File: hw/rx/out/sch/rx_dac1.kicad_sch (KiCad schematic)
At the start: 13 parts, among them U3 PCM5102A

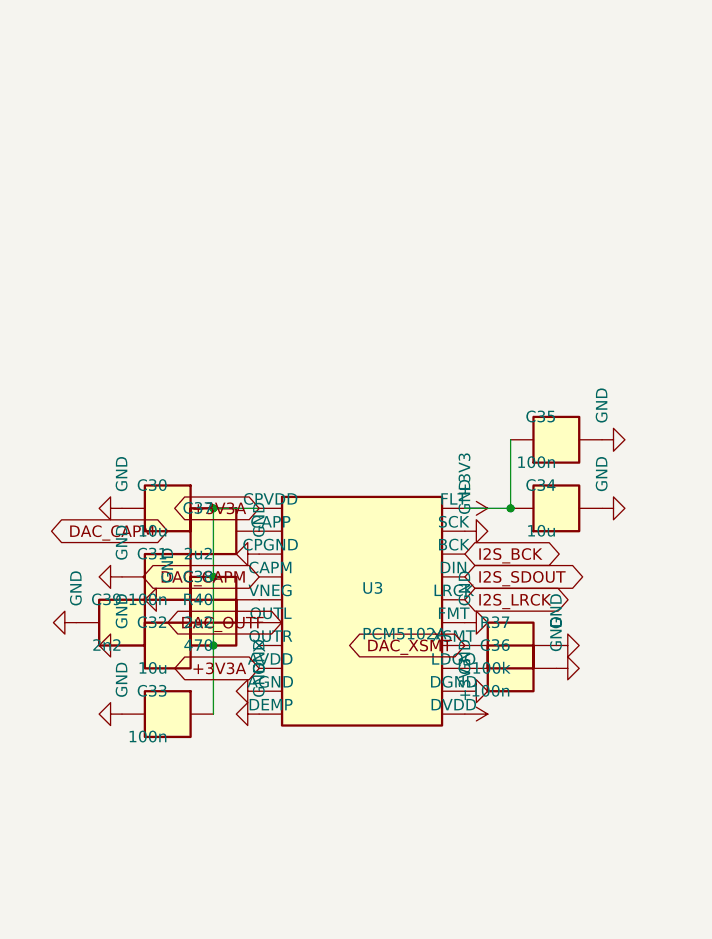
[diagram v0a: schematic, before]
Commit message: hw/rx: review fixes for #81 (mute relay + supervisor, S1J clamps, VCM discharge + 2-pole filter, 16 V LDOs, keyed header, I2S DNP, cable stability + power-cycle SPICE, FLT low latency) (#32)
Co-Authored-By: Claude Opus 5.5 <noreply@anthropic.com>
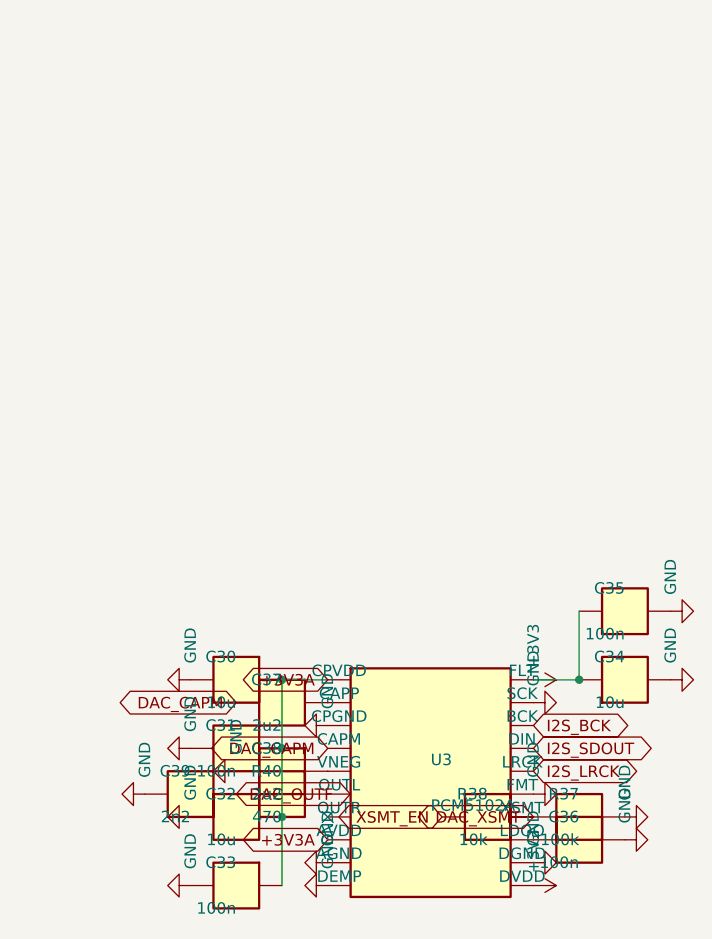
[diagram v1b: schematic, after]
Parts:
- added R38: 10k, Resistor_SMD:R_0402_1005Metric, symbol openpack_rx:R
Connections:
- net DAC_XSMT: now also R38.2
- new net XSMT_EN: R38.1
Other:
- moved on the sheet: C30, C31, C32, C33, C34, C35, C36, C37, C38, C39, R37, R40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

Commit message: hw/rx: receiver module BT40NE -> BT40E, FEM node pack-only (ADR-0021, #112)
- hw/rx: BT40E symbol (Fanstel v1.09 p.14 pad map = BT40F/NE names), footprint
  openpack:Fanstel_BT40E (14x16 mm), no FEM nets, P1.05 open; GPIO map unchanged.
  ERC 0/0. BOM: Digi-Key UK GBP 9.7765 q100 -> $30.68 / GBP 23.38 per sub-board.
- fw: receiver builds add boards/role_rx_cpunet.overlay (FEM node disabled, no
  &radio fem); rx.c refuses to build with the FEM enabled.
- ADR-0014 amended (datasheet checks, FCC X8WBT40F, no UKCA DoC, BOM).

Co-Authored-By: Claude Opus 5.5 <noreply@anthropic.com>
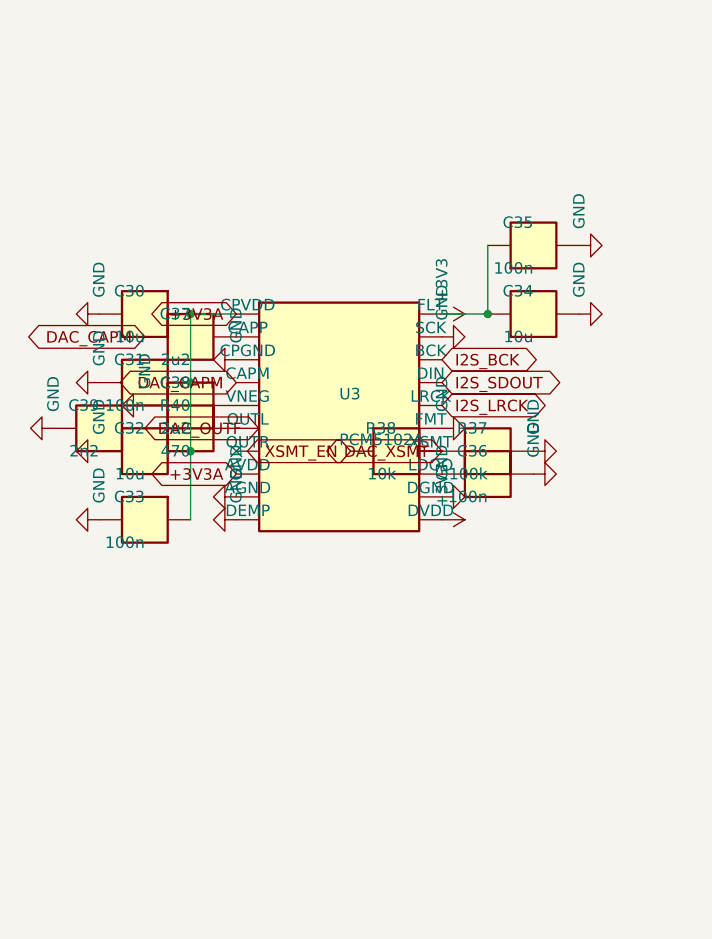
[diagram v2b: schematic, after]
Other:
- moved on the sheet: C30, C31, C32, C33, C34, C35, C36, C37, C38, C39, R37, R38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

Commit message: hw/rx: receiver sub-board layout, 50 ohm GCPW, keyed J1, JLC rules that load, fab outputs (#34) (#116)
Part of #34. Receiver layout (48x90 mm, DRC 0/0), #116 independent-review fixes (netclass pour clearances in rx + pack, no hole at J1 pin 14, solid RF grounds, K1 pin-1/CPL), every placed part with a checked LCSC code.

Co-Authored-By: Claude Opus 5.5 <noreply@anthropic.com>
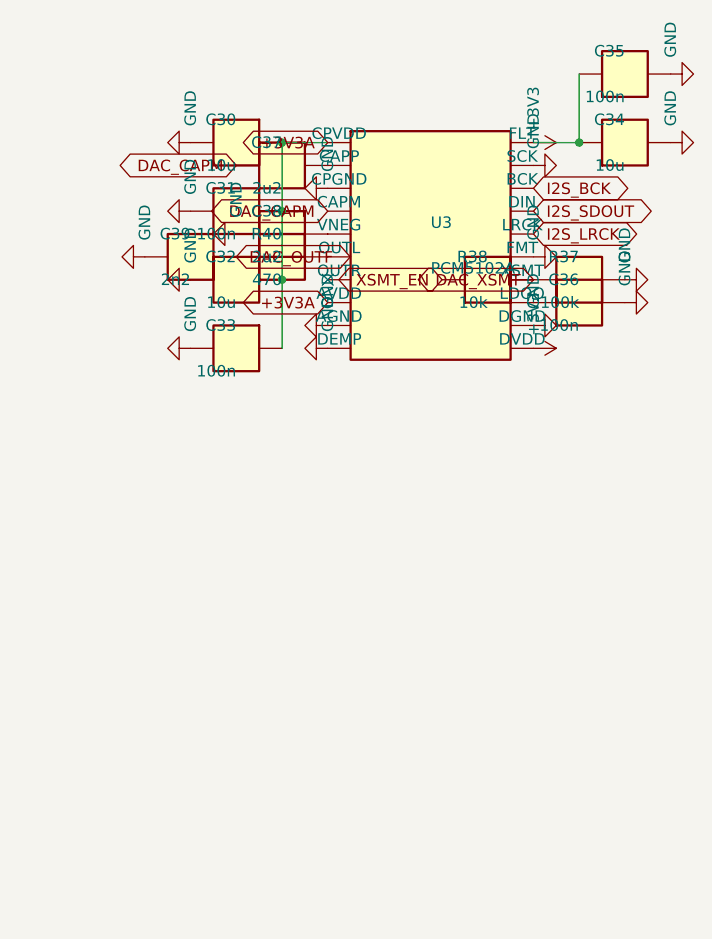
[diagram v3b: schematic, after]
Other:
- moved on the sheet: C30, C31, C32, C33, C34, C35, C36, C37, C38, C39, R37, R38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
